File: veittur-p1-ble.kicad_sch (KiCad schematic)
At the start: 21 parts, among them J1 Connector_HAN_P1, J2 Conn_01x06, Q1 BSS138, Q2 BSS138, U1 MIC5504-3.3YM5, U2 CH582F, U3 74AHCT1G125, Y1 32M, Y2 32k

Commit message: initial "complete"
is that it? should I just order this then?
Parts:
- removed AE1: Antenna_Dipole, RF_Antenna:Texas_SWRA117D_2.4GHz_Right, symbol Device:Antenna_Dipole
- removed D1: WS2812B, LED_SMD:LED_WS2812B_PLCC4_5.0x5.0mm_P3.2mm, symbol LED:WS2812B
- removed R3: 10k, Resistor_SMD:R_0603_1608Metric, symbol Device:R_Small
- removed U3: 74AHCT1G125, Package_TO_SOT_SMD:SOT-23-5, symbol karl-parts:74AHCT1G125
- added AE1: Antenna_Loop, wch-antenna:ANT-F-1-2.4G-1.6MM-FR4-WCH-FLIP, symbol Device:Antenna_Loop
- added D1: WS2812C-2020, LED_SMD:LED_WS2812-2020-PLCC4_2.0x2.0mm, symbol LED:SK6812MINI
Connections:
- net +5V: now also D1.4 (VDD)
- net GND: now also U2.29 (GND), AE1.2, D1.2 (VSS); no longer U2.0 (GND)
- net LED_OUT3V3: now also D1.3 (DIN)
- net at U2.21 (ANT): now also AE1.1
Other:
- note added: "General Purpose Indicator"
- note removed: "GP Indicator"

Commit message: add fixit notes for future revs
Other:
- note added: "FIXME - bring out reset to a pad for shorting at least, so we can bootloader it?"
- note added: "FIXME - need to put the led on spi data out bitbanging failed hard, and the uart doesn't offer inversion.."
- note added: "YOU FUCKING MORON you've used RXD0 twice! you _can_ keep using this to eval the hardware because we're never rx-ing from the user at this stage.."
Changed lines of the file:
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@@
+    (effects (font (size 1.27 1.27)) (justify left bottom))
+  )
+  (text "FIXME - need to put the led on spi data out\nbitbanging failed hard,\nand the uart doesn't offer inversion.."
+    (at 198.12 71.12 0)
+    (effects (font (size 1.27 1.27)) (justify left bottom))
+  )
+  (text "YOU FUCKING MORON\nyou've used RXD0 twice!\nyou _can_ keep using this to eval\nthe hardware because we're never \nrx-ing from the user at this stage.."
+    (at 220.98 63.5 0)
     (effects (font (size 1.27 1.27)) (justify left bottom))
   )
@@
     (effects (font (size 1.27 1.27)) (justify left bottom))
   )
+  (text "FIXME - bring out reset to a pad for shorting at least, so we can bootloader it?"
+    (at 187.96 144.78 0)
+    (effects (font (size 1.27 1.27)) (justify left bottom))
+  )

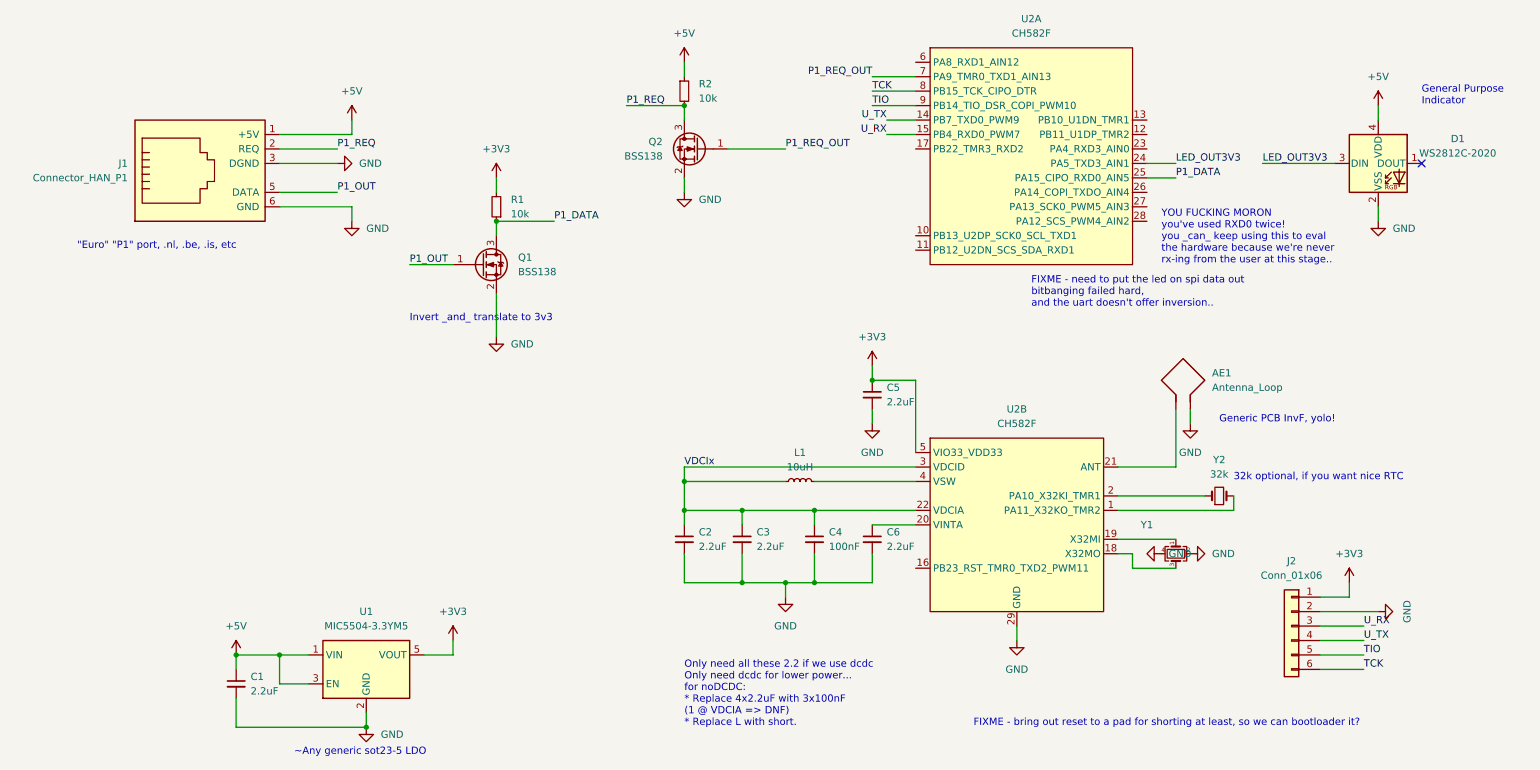
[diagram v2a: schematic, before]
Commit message: sch: "fix" "most" fixmes...
needs review and footprint assignments
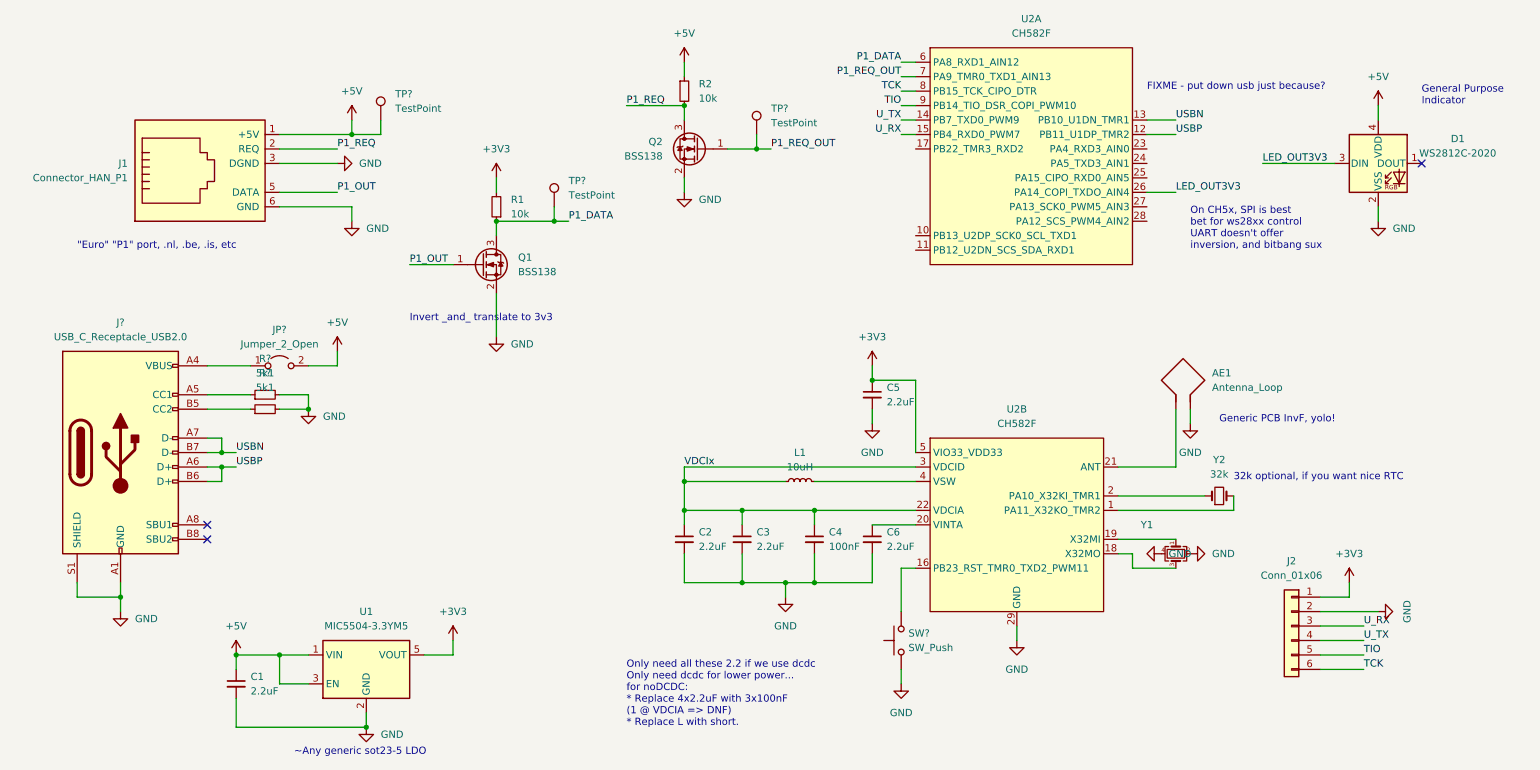
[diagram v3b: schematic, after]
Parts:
- added J?: USB_C_Receptacle_USB2.0, symbol Connector:USB_C_Receptacle_USB2.0
- added JP?: Jumper_2_Open, symbol Jumper:Jumper_2_Open
- added R? (x2): 5k1, symbol Device:R_Small
- added SW?: SW_Push, symbol Switch:SW_Push
- added TP? (x3): TestPoint, symbol Connector:TestPoint
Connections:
- net +5V: now also JP?.2 (B), TP?.1
- net GND: now also J?.A1 (GND), J?.A12 (GND), J?.B1 (GND), J?.B12 (GND), J?.S1 (SHIELD), R?.2, R?.2, SW?.1
- net LED_OUT3V3: now also U2.26 (PA14_COPI_TXDO_AIN4); no longer U2.24 (PA5_TXD3_AIN1)
- net P1_DATA: now also U2.6 (PA8_RXD1_AIN12), TP?.1; no longer U2.25 (PA15_CIPO_RXD0_AIN5)
- net P1_REQ_OUT: now also TP?.1
- net USBP: now reaches U2.12 (PB11_U1DP_TMR2)
- net USBP: now also J?.A6 (D+), J?.B6 (D+)
- net USBN: now reaches U2.13 (PB10_U1DN_TMR1)
- net USBN: now also J?.A7 (D-), J?.B7 (D-)
- net at U2.16 (PB23_RST_TMR0_TXD2_PWM11): now also SW?.2
- new net: J?.A5 (CC1), R?.1
- new net: J?.A4 (VBUS), J?.A9 (VBUS), J?.B4 (VBUS), J?.B9 (VBUS), JP?.1 (A)
- new net: J?.B5 (CC2), R?.1
- no-connect marks 1 -> 3
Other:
- note added: "FIXME - put down usb just because?"
- note added: "On CH5x, SPI is best bet for ws28xx control UART doesn't offer inversion, and bitbang sux"
- note removed: "FIXME - bring out reset to a pad for shorting at least, so we can bootloader it?"
- note removed: "FIXME - need to put the led on spi data out bitbanging failed hard, and the uart doesn't offer inversion.."
- note removed: "YOU FUCKING MORON you've used RXD0 twice! you _can_ keep using this to eval the hardware because we're never rx-ing from the user at this stage.."

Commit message: overhaul for jlc assembly
parts changes, revised layout, added the usb connector, just for fun...
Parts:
- removed R? (x2): 5k1, symbol Device:R_Small
- removed TP?: TestPoint, symbol Connector:TestPoint
- added R1, R2, R3, R4: 10k, Resistor_SMD:R_0603_1608Metric, symbol Device:R_Small
- added R7: 0, Resistor_SMD:R_0603_1608Metric, symbol Device:R_Small
- C1, C2, C3, C5, C6: MPN CL10A225KQ8NNNC -> CL10A225KO8NNNC; lcsc# (none) -> C23630
- C4: MPN (none) -> CC0603KRX7R9BB104; lcsc# (none) -> C14663
- D1: value WS2812C-2020 -> WS2812B-V5/W; footprint LED_SMD:LED_WS2812-2020-PLCC4_2.0x2.0mm -> LED_SMD:LED_WS2812B_PLCC4_5.0x5.0mm_P3.2mm; MPN WS2812C-2020-V1 -> WS2812B-V5/W; lcsc# (none) -> C2874885
- J1: renamed from J?; footprint (none) -> Connector_USB:USB_C_Receptacle_XKB_U262-16XN-4BVC11; MPN (none) -> U262-161N-4BVC11; lcsc# (none) -> C319148
- JP1: renamed from JP?; footprint (none) -> Connector_PinHeader_2.54mm:PinHeader_2x01_P2.54mm_Vertical
- L1: footprint Inductor_SMD:L_0805_2012Metric -> et-parts:L_Changjiang_FNR252012S; MPN CMP201209XD100MT -> SWPA252012S100MT; lcsc# (none) -> C37428
- Q1, Q2: MPN HX2303A -> AP2302B; lcsc# (none) -> C406812
- R5: renamed from R1; MPN (none) -> 0603WAF1002T5E; lcsc# (none) -> C25804
- R6: renamed from R2; MPN (none) -> 0603WAF1002T5E; lcsc# (none) -> C25804
- SW1: renamed from SW?; footprint (none) -> Connector_PinHeader_1.27mm:PinHeader_2x01_P1.27mm_Vertical
- TP2, TP3: renamed from TP?; footprint (none) -> TestPoint:TestPoint_Pad_1.0x1.0mm
- U1: lcsc# (none) -> C347386
- U2: lcsc# (none) -> C3001175
- Y1: lcsc# (none) -> C337683
- Y2: lcsc# (none) -> C271654
- renumbered J1 to J2, J2 to J3
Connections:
- net GND: now also R1.1, R2.1, R3.1, R4.1
- net P1_REQ_OUT: now also U2.28 (PA12_SCS_PWM4_AIN2); no longer U2.7 (PA9_TMR0_TXD1_AIN13)
- net x32i: now reaches U2.2 (PA10_X32KI_TMR1), Y2.1
- net x32o: now reaches U2.1 (PA11_X32KO_TMR2), Y2.2
- net cc1: now reaches J1.A5 (CC1)
- net cc1: now also R3.2, R4.2
- net vbus: now reaches J1.A4 (VBUS), J1.A9 (VBUS), J1.B4 (VBUS), J1.B9 (VBUS), JP1.1 (A)
- net clki: now reaches U2.19 (X32MI), Y1.1
- net clko: now reaches U2.18 (X32MO), Y1.3
- net cc2: now reaches J1.B5 (CC2)
- net cc2: now also R1.2, R2.2
- net RST: now reaches SW1.2, U2.16 (PB23_RST_TMR0_TXD2_PWM11)
- net vinta: now reaches C6.1, U2.20 (VINTA)
- net at AE1.1: now also R7.1; no longer U2.21 (ANT)
- new net: R7.2, U2.21 (ANT)
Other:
- note added: "5.1k/10% is easy with 5k/1% BoM line reduction for great glory"
- note added: "This counts as a test pad too"
- note added: "XKB U262 GCT USB4105"
- note removed: "FIXME - put down usb just because?"

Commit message: finalize production for rev2.
parts all adjusted for JLCPCB, bom and position files all uploaded
happily.
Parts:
- added TP3: TestPoint, et-parts:TestPoint_Plated_Hole_0.6_D0.8mm, symbol Connector:TestPoint
- TP1: renamed from TP2; footprint TestPoint:TestPoint_Pad_1.0x1.0mm -> et-parts:TestPoint_Plated_Hole_0.6_D0.8mm
- TP2: renamed from TP3; footprint TestPoint:TestPoint_Pad_1.0x1.0mm -> et-parts:TestPoint_Plated_Hole_0.6_D0.8mm
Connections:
- net at D1.1 (DOUT): now also TP3.1
- no-connect marks 3 -> 2
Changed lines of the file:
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@@
   (junction (at 137.16 101.6) (diameter 0) (color 0 0 0 0)
   )
-  (no_connect (at 266.7 45.72))
   (no_connect (at 53.34 111.76))
   (no_connect (at 53.34 109.22))
@@
     (stroke (width 0) (type default) (color 0 0 0 0))
   )
+  (wire (pts (xy 266.7 45.72) (xy 271.78 45.72))
+    (stroke (width 0) (type default) (color 0 0 0 0))
+  )
   (wire (pts (xy 104.14 55.88) (xy 114.3 55.88))
     (stroke (width 0) (type default) (color 0 0 0 0))
@@
     (pin "2")
   )
+  (symbol (lib_id "Connector:TestPoint") (at 271.78 45.72 0) (unit 1)
+    (in_bom yes) (on_board yes) (fields_autoplaced)
+    (property "Reference" "TP3" (id 0) (at 274.32 41.1479 0)
+      (effects (font (size 1.27 1.27)) (justify left))
+    )
+    (property "Value" "TestPoint" (id 1) (at 274.32 43.6879 0)
+      (effects (font (size 1.27 1.27)) (justify left))
+    )
+    (property "Footprint" "et-parts:TestPoint_Plated_Hole_0.6_D0.8mm" (id 2) (at 276.86 45.72 0)
+      (effects (font (size 1.27 1.27)) hide)
+    )
+    (property "Datasheet" "~" (id 3) (at 276.86 45.72 0)
+      (effects (font (size 1.27 1.27)) hide)
+    )
+    (pin "1")
+  )
   (symbol (lib_id "Connector:TestPoint") (at 114.3 53.34 0) (unit 1)
     (in_bom yes) (on_board yes) (fields_autoplaced)
-    (property "Reference" "TP2" (id 0) (at 116.84 48.7679 0)
+    (property "Reference" "TP1" (id 0) (at 116.84 48.7679 0)
       (effects (font (size 1.27 1.27)) (justify left))
     )
@@
       (effects (font (size 1.27 1.27)) (justify left))
     )
-    (property "Footprint" "TestPoint:TestPoint_Pad_1.0x1.0mm" (id 2) (at 119.38 53.34 0)
+    (property "Footprint" "et-parts:TestPoint_Plated_Hole_0.6_D0.8mm" (id 2) (at 119.38 53.34 0)
       (effects (font (size 1.27 1.27)) hide)
     )
@@
   (symbol (lib_id "Connector:TestPoint") (at 149.86 40.64 0) (unit 1)
     (in_bom yes) (on_board yes) (fields_autoplaced)
-    (property "Reference" "TP3" (id 0) (at 152.4 36.0679 0)
+    (property "Reference" "TP2" (id 0) (at 152.4 36.0679 0)
       (effects (font (size 1.27 1.27)) (justify left))
     )
@@
       (effects (font (size 1.27 1.27)) (justify left))
     )
-    (property "Footprint" "TestPoint:TestPoint_Pad_1.0x1.0mm" (id 2) (at 154.94 40.64 0)
+    (property "Footprint" "et-parts:TestPoint_Plated_Hole_0.6_D0.8mm" (id 2) (at 154.94 40.64 0)
       (effects (font (size 1.27 1.27)) hide)
     )
@@
   )
   (symbol (lib_id "LED:SK6812MINI") (at 259.08 45.72 0) (unit 1)
-    (in_bom yes) (on_board yes) (fields_autoplaced)
-    (property "Reference" "D1" (id 0) (at 273.05 41.3893 0))
-    (property "Value" "WS2812B-V5/W" (id 1) (at 273.05 43.9293 0))
+    (in_bom yes) (on_board yes)
+    (property "Reference" "D1" (id 0) (at 264.16 38.1 0))
+    (property "Value" "WS2812B-V5/W" (id 1) (at 269.24 53.34 0))
     (property "Footprint" "LED_SMD:LED_WS2812B_PLCC4_5.0x5.0mm_P3.2mm" (id 2) (at 260.35 53.34 0)
       (effects (font (size 1.27 1.27)) (justify left top) hide)
@@
     )
     (path "/3879c455-8cea-401f-a5b1-0e9c4df12d3c"
-      (reference "TP2") (unit 1) (value "TestPoint") (footprint "TestPoint:TestPoint_Pad_1.0x1.0mm")
+      (reference "TP1") (unit 1) (value "TestPoint") (footprint "et-parts:TestPoint_Plated_Hole_0.6_D0.8mm")
     )
     (path "/3ac3aafd-bb25-4e2d-8d34-dee7c613745a"
-      (reference "TP3") (unit 1) (value "TestPoint") (footprint "TestPoint:TestPoint_Pad_1.0x1.0mm")
+      (reference "TP2") (unit 1) (value "TestPoint") (footprint "et-parts:TestPoint_Plated_Hole_0.6_D0.8mm")
+    )
+    (path "/3337ff0b-7442-4316-a9f8-568a08c31c74"
+      (reference "TP3") (unit 1) (value "TestPoint") (footprint "et-parts:TestPoint_Plated_Hole_0.6_D0.8mm")
     )
     (path "/66a182eb-2a0e-416b-b875-2b9fdc032f69"

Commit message: Generate new pdfs and set page settings
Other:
- company: (none) -> Ekta Labs
- title: (none) -> Euro P1/HAN to BLE dongle
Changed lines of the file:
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@@
 (kicad_sch (version 20211123) (generator eeschema)
   (paper "A4")
+  (title_block
+    (title "Euro P1/HAN to BLE dongle")
+    (date "2022-10-07")
+    (rev "2022-10")
+    (company "Ekta Labs")
+    (comment 1 "Karl Palsson")
+    (comment 2 "false.ekta.is")
+  )
   (junction (at 55.88 96.52) (diameter 0) (color 0 0 0 0)
   )
